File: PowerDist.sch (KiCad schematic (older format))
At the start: 13 parts

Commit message: Adds logic analyzer points and LEDs
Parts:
- D?: If (none) -> 2mA; Vf (none) -> 1.9V
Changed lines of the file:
@@
 F 4 "Green" V 6350 3600 50  0001 C CNN "Color"
 F 5 "APTD2012LCGCK" V 6350 3600 50  0001 C CNN "P/N"
+F 6 "1.9V" V 6350 3600 50  0001 C CNN "Vf"
+F 7 "2mA" V 6350 3600 50  0001 C CNN "If"
 	1    6350 3600
 	0    -1   -1   0

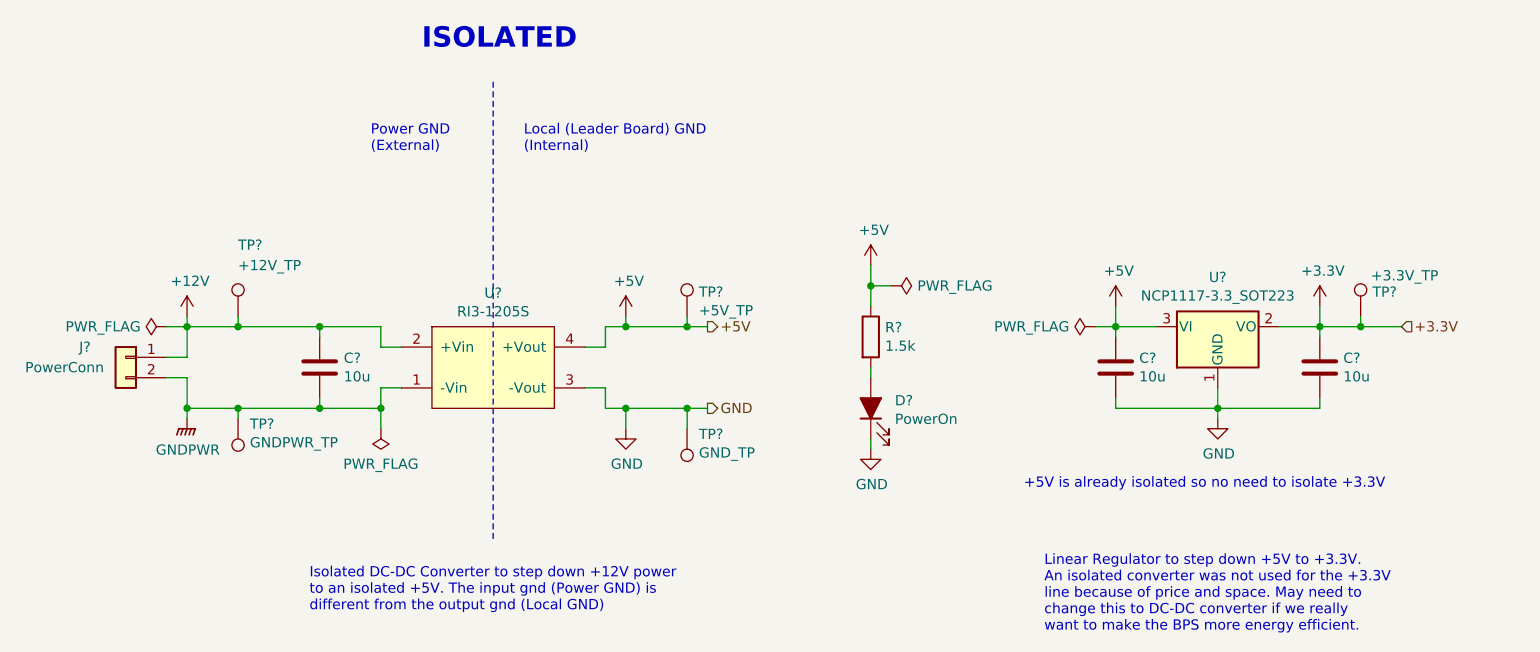
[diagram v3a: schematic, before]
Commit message: Initial layout of the Telemtry board.
The ethernet interface needs more work.
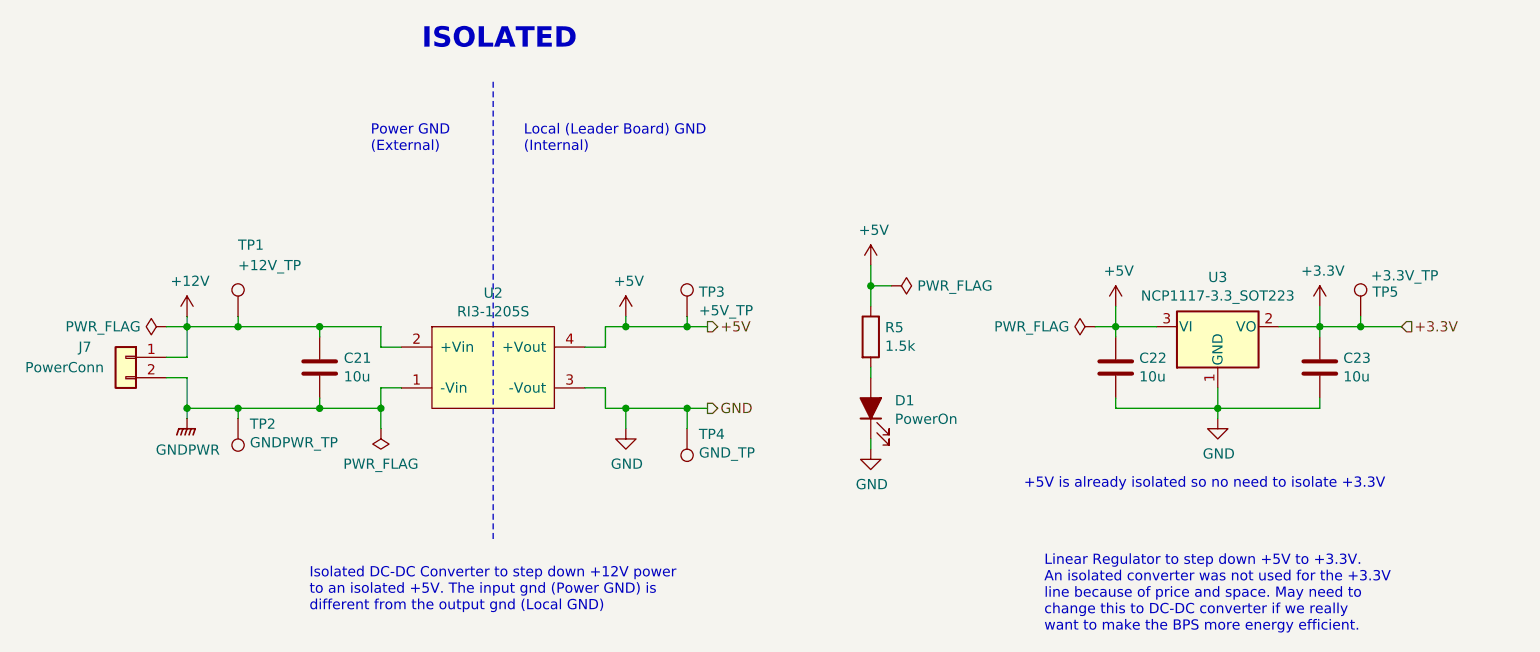
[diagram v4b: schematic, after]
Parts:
- gave numbers to parts that had none: 13
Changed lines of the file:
@@
 $EndDescr
 $Comp
-L power:+12V #PWR?
+L power:+12V #PWR0123
 U 1 1 5C35F2D2
 P 3000 3150
-F 0 "#PWR?" H 3000 3000 50  0001 C CNN
+F 0 "#PWR0123" H 3000 3000 50  0001 C CNN
 F 1 "+12V" H 3015 3323 50  0000 C CNN
 F 2 "" H 3000 3150 50  0001 C CNN
@@
 	3000 3600 3000 3650
 $Comp
-L Device:C C?
+L Device:C C21
 U 1 1 5C35F7E4
 P 3650 3400
-F 0 "C?" H 3768 3446 50  0000 L CNN
+F 0 "C21" H 3768 3446 50  0000 L CNN
 F 1 "10u" H 3768 3355 50  0000 L CNN
 F 2 "UTSVT_Passive:C_2220_5750Metric" H 3688 3250 50  0001 C CNN
@@
 +5V
 $Comp
-L power:+5V #PWR?
+L power:+5V #PWR0124
 U 1 1 5C376123
 P 5150 3150
-F 0 "#PWR?" H 5150 3000 50  0001 C CNN
+F 0 "#PWR0124" H 5150 3000 50  0001 C CNN
 F 1 "+5V" H 5165 3323 50  0000 C CNN
 F 2 "" H 5150 3150 50  0001 C CNN
@@
 $EndComp
 $Comp
-L Connector:TestPoint TP?
+L Connector:TestPoint TP1
 U 1 1 5C37D606
 P 3250 3150
-F 0 "TP?" H 3250 3500 50  0000 L CNN
+F 0 "TP1" H 3250 3500 50  0000 L CNN
 F 1 "+12V_TP" H 3250 3400 50  0000 L CNN
 F 2 "TestPoint:TestPoint_Keystone_5005-5009_Compact" H 3450 3150 50  0001 C CNN
@@
 	3250 3150 3250 3200
 $Comp
-L Connector:TestPoint TP?
+L Connector:TestPoint TP3
 U 1 1 5C37E6A3
 P 5450 3150
-F 0 "TP?" H 5508 3270 50  0000 L CNN
+F 0 "TP3" H 5508 3270 50  0000 L CNN
 F 1 "+5V_TP" H 5508 3179 50  0000 L CNN
 F 2 "TestPoint:TestPoint_Keystone_5005-5009_Compact" H 5650 3150 50  0001 C CNN
@@
 	5450 3150 5450 3200
 $Comp
-L Connector:TestPoint TP?
+L Connector:TestPoint TP4
 U 1 1 5C37F6B1
 P 5450 3700
-F 0 "TP?" H 5392 3727 50  0000 R CNN
+F 0 "TP4" H 5392 3727 50  0000 R CNN
 F 1 "GND_TP" H 5392 3818 50  0000 R CNN
 F 2 "TestPoint:TestPoint_Keystone_5005-5009_Compact" H 5650 3700 50  0001 C CNN
@@
 	5450 3700 5450 3600
 $Comp
-L power:GND #PWR?
+L power:GND #PWR0125
 U 1 1 5C58D746
 P 6350 3800
-F 0 "#PWR?" H 6350 3550 50  0001 C CNN
+F 0 "#PWR0125" H 6350 3550 50  0001 C CNN
 F 1 "GND" H 6355 3627 50  0000 C CNN
 F 2 "" H 6350 3800 50  0001 C CNN
@@
 $EndComp
 $Comp
-L Device:LED_ALT D?
+L Device:LED_ALT D1
 U 1 1 5C58D83E
 P 6350 3600
-F 0 "D?" V 6388 3482 50  0000 R CNN
+F 0 "D1" V 6388 3482 50  0000 R CNN
 F 1 "PowerOn" V 6297 3482 50  0000 R CNN
 F 2 "LED_SMD:LED_0805_2012Metric" H 6350 3600 50  0001 C CNN
@@
 $EndComp
 $Comp
-L Device:R R?
+L Device:R R5
 U 1 1 5C58D993
 P 6350 3250
-F 0 "R?" H 6420 3296 50  0000 L CNN
+F 0 "R5" H 6420 3296 50  0000 L CNN
 F 1 "1.5k" H 6420 3205 50  0000 L CNN
 F 2 "Resistor_SMD:R_0805_2012Metric" V 6280 3250 50  0001 C CNN
@@
 	6350 3450 6350 3400
 $Comp
-L power:+5V #PWR?
+L power:+5V #PWR0126
 U 1 1 5C58FEF6
 P 6350 2900
-F 0 "#PWR?" H 6350 2750 50  0001 C CNN
+F 0 "#PWR0126" H 6350 2750 50  0001 C CNN
 F 1 "+5V" H 6365 3073 50  0000 C CNN
 F 2 "" H 6350 2900 50  0001 C CNN
@@
 	6350 2900 6350 3000
 $Comp
-L power:GND #PWR?
+L power:GND #PWR0127
 U 1 1 5C3F3B1F
 P 5150 3700
-F 0 "#PWR?" H 5150 3450 50  0001 C CNN
+F 0 "#PWR0127" H 5150 3450 50  0001 C CNN
 F 1 "GND" H 5155 3527 50  0000 C CNN
 F 2 "" H 5150 3700 50  0001 C CNN
@@
 $EndComp
 $Comp
-L power:GNDPWR #PWR?
+L power:GNDPWR #PWR0128
 U 1 1 5C3F7204
 P 3000 3650
-F 0 "#PWR?" H 3000 3450 50  0001 C CNN
+F 0 "#PWR0128" H 3000 3450 50  0001 C CNN
 F 1 "GNDPWR" H 3004 3496 50  0000 C CNN
 F 2 "" H 3000 3600 50  0001 C CNN
@@
 $EndComp
 $Comp
-L power:+5V #PWR?
+L power:+5V #PWR0129
 U 1 1 5C702374
 P 7550 3100
-F 0 "#PWR?" H 7550 2950 50  0001 C CNN
+F 0 "#PWR0129" H 7550 2950 50  0001 C CNN
 F 1 "+5V" H 7565 3273 50  0000 C CNN
 F 2 "" H 7550 3100 50  0001 C CNN
@@
 $EndComp
 $Comp
-L Regulator_Linear:LD1117S33TR_SOT223 U?
+L Regulator_Linear:LD1117S33TR_SOT223 U3
 U 1 1 5C70247C
 P 8050 3200
-F 0 "U?" H 8050 3442 50  0000 C CNN
+F 0 "U3" H 8050 3442 50  0000 C CNN
 F 1 "NCP1117-3.3_SOT223" H 8050 3351 50  0000 C CNN
 F 2 "Package_TO_SOT_SMD:SOT-223-3_TabPin2" H 8050 3400 50  0001 C CNN
@@
 $EndComp
 $Comp
-L Device:C C?
+L Device:C C22
 U 1 1 5C702937
 P 7550 3400
-F 0 "C?" H 7665 3446 50  0000 L CNN
+F 0 "C22" H 7665 3446 50  0000 L CNN
 F 1 "10u" H 7665 3355 50  0000 L CNN
 F 2 "Capacitor_SMD:C_0805_2012Metric" H 7588 3250 50  0001 C CNN
@@
 $EndComp
 $Comp
-L Device:C C?
+L Device:C C23
 U 1 1 5C7029C7
 P 8550 3400
-F 0 "C?" H 8665 3446 50  0000 L CNN
+F 0 "C23" H 8665 3446 50  0000 L CNN
 F 1 "10u" H 8665 3355 50  0000 L CNN
 F 2 "Capacitor_SMD:C_0805_2012Metric" H 8588 3250 50  0001 C CNN
@@
 	8550 3200 8550 3250
 $Comp
-L power:GND #PWR?
+L power:GND #PWR0130
 U 1 1 5C703BF4
 P 8050 3650
-F 0 "#PWR?" H 8050 3400 50  0001 C CNN
+F 0 "#PWR0130" H 8050 3400 50  0001 C CNN
 F 1 "GND" H 8055 3477 50  0000 C CNN
 F 2 "" H 8050 3650 50  0001 C CNN
@@
 Connection ~ 7550 3200
 $Comp
-L power:+3.3V #PWR?
+L power:+3.3V #PWR0131
 U 1 1 5C7065C8
 P 8550 3100
-F 0 "#PWR?" H 8550 2950 50  0001 C CNN
+F 0 "#PWR0131" H 8550 2950 50  0001 C CNN
 F 1 "+3.3V" H 8565 3273 50  0000 C CNN
 F 2 "" H 8550 3100 50  0001 C CNN
@@
 	8950 3200 8750 3200
 $Comp
-L Connector:TestPoint TP?
+L Connector:TestPoint TP5
 U 1 1 5C708412
 P 8750 3150
-F 0 "TP?" H 8808 3270 50  0000 L CNN
+F 0 "TP5" H 8808 3270 50  0000 L CNN
 F 1 "+3.3V_TP" H 8800 3350 50  0000 L CNN
 F 2 "TestPoint:TestPoint_Keystone_5005-5009_Compact" H 8950 3150 50  0001 C CNN
@@
 	8750 3200 8550 3200
 $Comp
-L utsvt-power-regulators:RI3-1205S U?
+L utsvt-power-regulators:RI3-1205S U2
 U 1 1 5C38C4FE
 P 4500 3200
-F 0 "U?" H 4500 3365 50  0000 C CNN
+F 0 "U2" H 4500 3365 50  0000 C CNN
 F 1 "RI3-1205S" H 4500 3274 50  0000 C CNN
 F 2 "UTSVT_ICs:RI3_DC_Converter" H 4500 3200 50  0001 C CNN
@@
 	5450 3200 5550 3200
 $Comp
-L Connector:TestPoint TP?
+L Connector:TestPoint TP2
 U 1 1 5C82CEA3
 P 3250 3650
-F 0 "TP?" H 3192 3677 50  0000 R CNN
+F 0 "TP2" H 3192 3677 50  0000 R CNN
 F 1 "GNDPWR_TP" H 3192 3768 50  0000 R CNN
 F 2 "TestPoint:TestPoint_Keystone_5005-5009_Compact" H 3450 3650 50  0001 C CNN
@@
 +5V is already isolated so no need to isolate +3.3V
 $Comp
-L Connector_Generic:Conn_01x02 J?
+L Connector_Generic:Conn_01x02 J7
 U 1 1 5F1149C6
 P 2700 3350
-F 0 "J?" H 2900 3400 50  0000 C CNN
+F 0 "J7" H 2900 3400 50  0000 C CNN
 F 1 "PowerConn" H 3000 3300 50  0000 C CNN
 F 2 "UTSVT_Connectors:Molex_MicroFit3.0_1x2xP3.00mm_PolarizingPeg_Vertical" H 2700 3350 50  0001 C CNN
@@
 	3000 3200 3000 3350
 $Comp
-L power:PWR_FLAG #FLG?
+L power:PWR_FLAG #FLG0101
 U 1 1 5F1E78A7
 P 7450 3200
-F 0 "#FLG?" H 7450 3275 50  0001 C CNN
+F 0 "#FLG0101" H 7450 3275 50  0001 C CNN
 F 1 "PWR_FLAG" V 7450 3327 50  0000 L CNN
 F 2 "" H 7450 3200 50  0001 C CNN
@@
 	7450 3200 7550 3200
 $Comp
-L power:PWR_FLAG #FLG?
+L power:PWR_FLAG #FLG0102
 U 1 1 5F1EAFA2
 P 3950 3700
-F 0 "#FLG?" H 3950 3775 50  0001 C CNN
+F 0 "#FLG0102" H 3950 3775 50  0001 C CNN
 F 1 "PWR_FLAG" H 3950 3873 50  0000 C CNN
 F 2 "" H 3950 3700 50  0001 C CNN
@@
 $EndComp
 $Comp
-L power:PWR_FLAG #FLG?
+L power:PWR_FLAG #FLG0103
 U 1 1 5F1ED21F
 P 6450 3000
-F 0 "#FLG?" H 6450 3075 50  0001 C CNN
+F 0 "#FLG0103" H 6450 3075 50  0001 C CNN
 F 1 "PWR_FLAG" V 6450 3128 50  0000 L CNN
 F 2 "" H 6450 3000 50  0001 C CNN
@@
 	6350 3000 6350 3100
 $Comp
-L power:PWR_FLAG #FLG?
+L power:PWR_FLAG #FLG0104
 U 1 1 5F1F32D3
 P 2900 3200
-F 0 "#FLG?" H 2900 3275 50  0001 C CNN
+F 0 "#FLG0104" H 2900 3275 50  0001 C CNN
 F 1 "PWR_FLAG" V 2900 3327 50  0000 L CNN
 F 2 "" H 2900 3200 50  0001 C CNN
